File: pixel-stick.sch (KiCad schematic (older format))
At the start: 17 parts, among them J1 WS2811, J2 Conn_01x06, Q1 BSS138, U1 SPX3819M5-L-3-3, U2 RT9361AGE, U3 ESP-12E

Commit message: Layout board
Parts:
- C1: value 470µF -> 1000µF; footprint Capacitor_SMD:C_Elec_6.3x7.7 -> Capacitor_THT:CP_Radial_D10.0mm_P5.00mm
- J1: footprint Connector_Wire:SolderWirePad_1x03_P3.81mm_Drill1.2mm -> Connector_Wire:SolderWirePad_1x03_P3.175mm_Drill1mm
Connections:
- net +3V3: now also J2.2 (Pin_2); no longer J2.3 (Pin_3)
- net EN: now also J2.6 (Pin_6); no longer J2.2 (Pin_2)
- net GPIO0: now also J2.3 (Pin_3); no longer J2.6 (Pin_6)
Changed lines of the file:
@@
 EESchema Schematic File Version 4
 LIBS:pixel-stick-cache
-EELAYER 30 0
+EELAYER 29 0
 EELAYER END
 $Descr A4 11693 8268
@@
 P 5500 1750
 F 0 "C1" H 5615 1796 50  0000 L CNN
-F 1 "470µF" H 5615 1705 50  0000 L CNN
-F 2 "Capacitor_SMD:C_Elec_6.3x7.7" H 5500 1750 50  0001 C CNN
+F 1 "1000µF" H 5615 1705 50  0000 L CNN
+F 2 "Capacitor_THT:CP_Radial_D10.0mm_P5.00mm" H 5500 1750 50  0001 C CNN
 F 3 "~" H 5500 1750 50  0001 C CNN
 	1    5500 1750
@@
 F 0 "J1" H 2730 1642 50  0000 L CNN
 F 1 "WS2811" H 2730 1551 50  0000 L CNN
-F 2 "Connector_Wire:SolderWirePad_1x03_P3.81mm_Drill1.2mm" H 2650 1600 50  0001 C CNN
+F 2 "Connector_Wire:SolderWirePad_1x03_P3.175mm_Drill1mm" H 2650 1600 50  0001 C CNN
 F 3 "~" H 2650 1600 50  0001 C CNN
 	1    2650 1600
@@
 L power:+3.3V #PWR0106
 U 1 1 5E1A778D
-P 9700 4650
-F 0 "#PWR0106" H 9700 4500 50  0001 C CNN
-F 1 "+3.3V" V 9715 4778 50  0000 L CNN
-F 2 "" H 9700 4650 50  0001 C CNN
-F 3 "" H 9700 4650 50  0001 C CNN
-	1    9700 4650
+P 9700 4550
+F 0 "#PWR0106" H 9700 4400 50  0001 C CNN
+F 1 "+3.3V" V 9715 4678 50  0000 L CNN
+F 2 "" H 9700 4550 50  0001 C CNN
+F 3 "" H 9700 4550 50  0001 C CNN
+	1    9700 4550
 	0    -1   -1   0
 $EndComp
@@
 	10000 4450 9700 4450
 Wire Wire Line
+	10000 4550 9700 4550
+Wire Wire Line
+	10000 4950 9700 4950
+Wire Wire Line
+	10000 4750 9700 4750
+Wire Wire Line
+	10000 4850 9700 4850
+Wire Wire Line
 	10000 4650 9700 4650
-Wire Wire Line
-	10000 4550 9700 4550
-Wire Wire Line
-	10000 4750 9700 4750
-Wire Wire Line
-	10000 4850 9700 4850
-Wire Wire Line
-	10000 4950 9700 4950
 Text Label 9700 4750 0    50   ~ 0
 RXD
 Text Label 9700 4850 0    50   ~ 0
 TXD
-Text Label 9700 4550 0    50   ~ 0
+Text Label 9700 4950 0    50   ~ 0
 EN
-Text Label 9700 4950 0    50   ~ 0
+Text Label 9700 4650 0    50   ~ 0
 GPIO0
 Text Notes 9250 5500 0    157  ~ 0

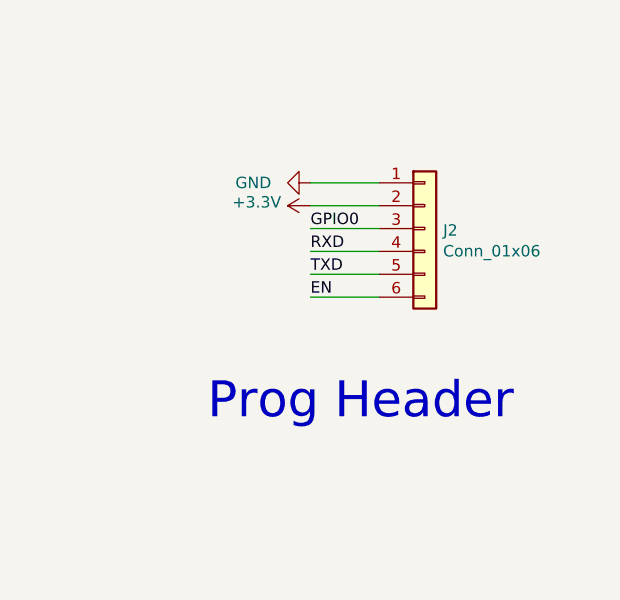
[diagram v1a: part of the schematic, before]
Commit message: revise board for testing
use the ESP-01 socket for most test points, added a 5V test point and changed the wire solder pads for 2.54mm pitch. Also added mounting (guide) holes for a test jig
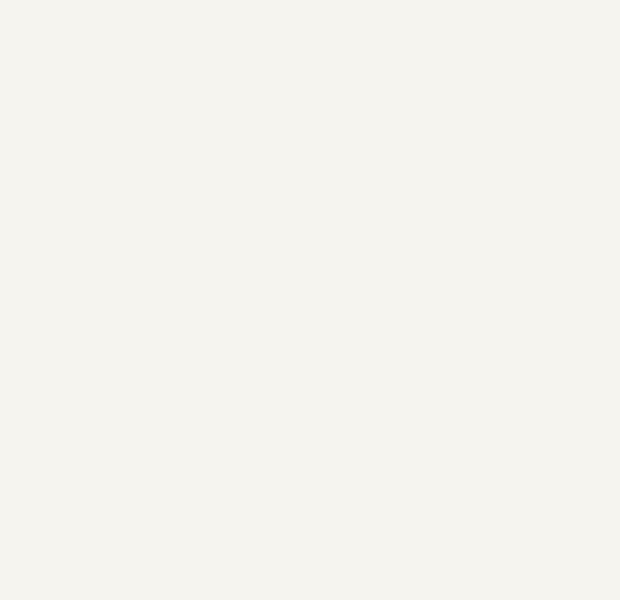
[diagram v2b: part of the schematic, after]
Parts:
- removed J2: Conn_01x06, Connector_PinHeader_2.54mm:PinHeader_1x06_P2.54mm_Vertical, symbol Connector_Generic:Conn_01x06
- J1: footprint Connector_Wire:SolderWirePad_1x03_P3.175mm_Drill1mm -> Connector_PinHeader_2.54mm:PinHeader_1x03_P2.54mm_Vertical
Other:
- note removed: "Prog Header"
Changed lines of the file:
@@
 EESchema Schematic File Version 4
 LIBS:pixel-stick-cache
-EELAYER 29 0
+EELAYER 30 0
 EELAYER END
 $Descr A4 11693 8268
@@
 F 0 "J1" H 2730 1642 50  0000 L CNN
 F 1 "WS2811" H 2730 1551 50  0000 L CNN
-F 2 "Connector_Wire:SolderWirePad_1x03_P3.175mm_Drill1mm" H 2650 1600 50  0001 C CNN
+F 2 "Connector_PinHeader_2.54mm:PinHeader_1x03_P2.54mm_Vertical" H 2650 1600 50  0001 C CNN
 F 3 "~" H 2650 1600 50  0001 C CNN
 	1    2650 1600
@@
 	1    0    0    -1
 $EndComp
-$Comp
-L Connector_Generic:Conn_01x06 J2
-U 1 1 5E1A6B59
-P 10200 4650
-F 0 "J2" H 10280 4642 50  0000 L CNN
-F 1 "Conn_01x06" H 10280 4551 50  0000 L CNN
-F 2 "Connector_PinHeader_2.54mm:PinHeader_1x06_P2.54mm_Vertical" H 10200 4650 50  0001 C CNN
-F 3 "~" H 10200 4650 50  0001 C CNN
-	1    10200 4650
-	1    0    0    -1
-$EndComp
-$Comp
-L power:+3.3V #PWR0106
-U 1 1 5E1A778D
-P 9700 4550
-F 0 "#PWR0106" H 9700 4400 50  0001 C CNN
-F 1 "+3.3V" V 9715 4678 50  0000 L CNN
-F 2 "" H 9700 4550 50  0001 C CNN
-F 3 "" H 9700 4550 50  0001 C CNN
-	1    9700 4550
-	0    -1   -1   0
-$EndComp
-$Comp
-L power:GND #PWR0107
-U 1 1 5E1A8422
-P 9700 4450
-F 0 "#PWR0107" H 9700 4200 50  0001 C CNN
-F 1 "GND" V 9700 4200 50  0000 C CNN
-F 2 "" H 9700 4450 50  0001 C CNN
-F 3 "" H 9700 4450 50  0001 C CNN
-	1    9700 4450
-	0    1    1    0
-$EndComp
-Wire Wire Line
-	10000 4450 9700 4450
-Wire Wire Line
-	10000 4550 9700 4550
-Wire Wire Line
-	10000 4950 9700 4950
-Wire Wire Line
-	10000 4750 9700 4750
-Wire Wire Line
-	10000 4850 9700 4850
-Wire Wire Line
-	10000 4650 9700 4650
-Text Label 9700 4750 0    50   ~ 0
-RXD
-Text Label 9700 4850 0    50   ~ 0
-TXD
-Text Label 9700 4950 0    50   ~ 0
-EN
-Text Label 9700 4650 0    50   ~ 0
-GPIO0
-Text Notes 9250 5500 0    157  ~ 0
-Prog Header
 Wire Wire Line
 	4300 3850 4650 3850

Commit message: shrink board
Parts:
- C1: value 1000µF -> 100µF; footprint Capacitor_THT:CP_Radial_D10.0mm_P5.00mm -> Capacitor_SMD:CP_Elec_6.3x7.7
- C2: value 1µF -> 10µF 16V
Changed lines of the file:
@@
 EESchema Schematic File Version 4
 LIBS:pixel-stick-cache
-EELAYER 30 0
+EELAYER 29 0
 EELAYER END
 $Descr A4 11693 8268
@@
 P 6300 1700
 F 0 "C2" H 6415 1746 50  0000 L CNN
-F 1 "1µF" H 6415 1655 50  0000 L CNN
+F 1 "10µF 16V" H 6415 1655 50  0000 L CNN
 F 2 "Capacitor_SMD:C_0805_2012Metric" H 6338 1550 50  0001 C CNN
 F 3 "~" H 6300 1700 50  0001 C CNN
@@
 P 5500 1750
 F 0 "C1" H 5615 1796 50  0000 L CNN
-F 1 "1000µF" H 5615 1705 50  0000 L CNN
-F 2 "Capacitor_THT:CP_Radial_D10.0mm_P5.00mm" H 5500 1750 50  0001 C CNN
+F 1 "100µF" H 5615 1705 50  0000 L CNN
+F 2 "Capacitor_SMD:CP_Elec_6.3x7.7" H 5500 1750 50  0001 C CNN
 F 3 "~" H 5500 1750 50  0001 C CNN
 	1    5500 1750

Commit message: rev 2.0a
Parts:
- J1: footprint Connector_PinHeader_2.54mm:PinHeader_1x03_P2.54mm_Vertical -> Connector_Wire:SolderWirePad_1x03_P3.175mm_Drill1mm
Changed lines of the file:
@@
 F 0 "J1" H 2730 1642 50  0000 L CNN
 F 1 "WS2811" H 2730 1551 50  0000 L CNN
-F 2 "Connector_PinHeader_2.54mm:PinHeader_1x03_P2.54mm_Vertical" H 2650 1600 50  0001 C CNN
+F 2 "Connector_Wire:SolderWirePad_1x03_P3.175mm_Drill1mm" H 2650 1600 50  0001 C CNN
 F 3 "~" H 2650 1600 50  0001 C CNN
 	1    2650 1600

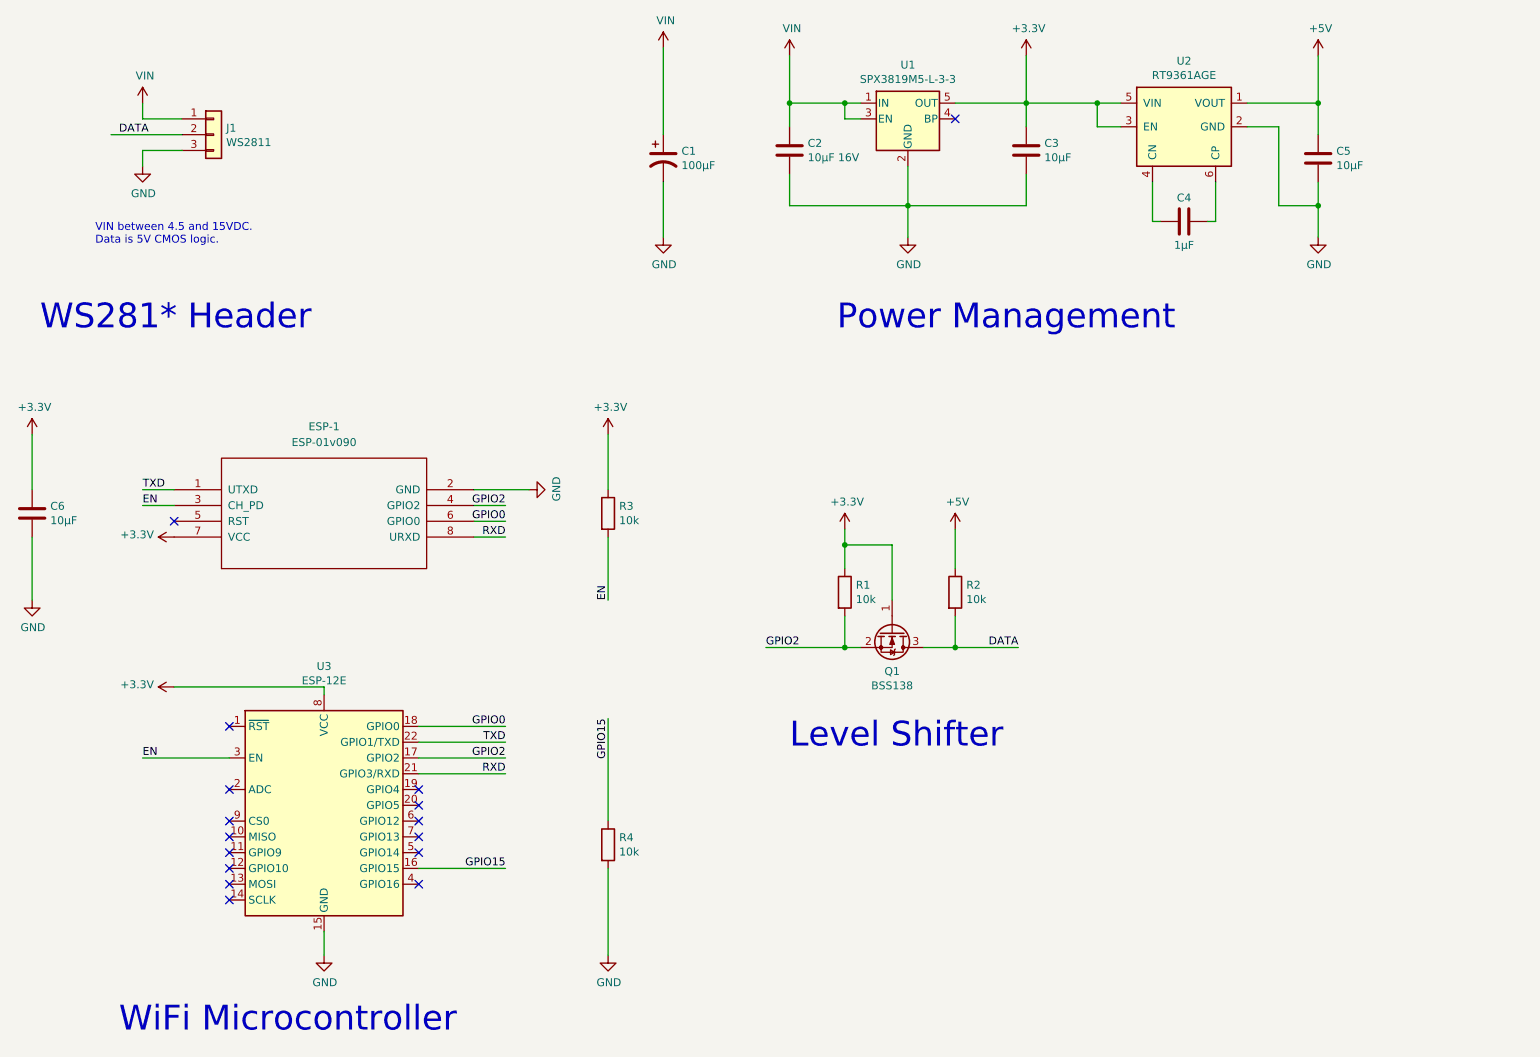
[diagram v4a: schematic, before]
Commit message: utilize level shifter
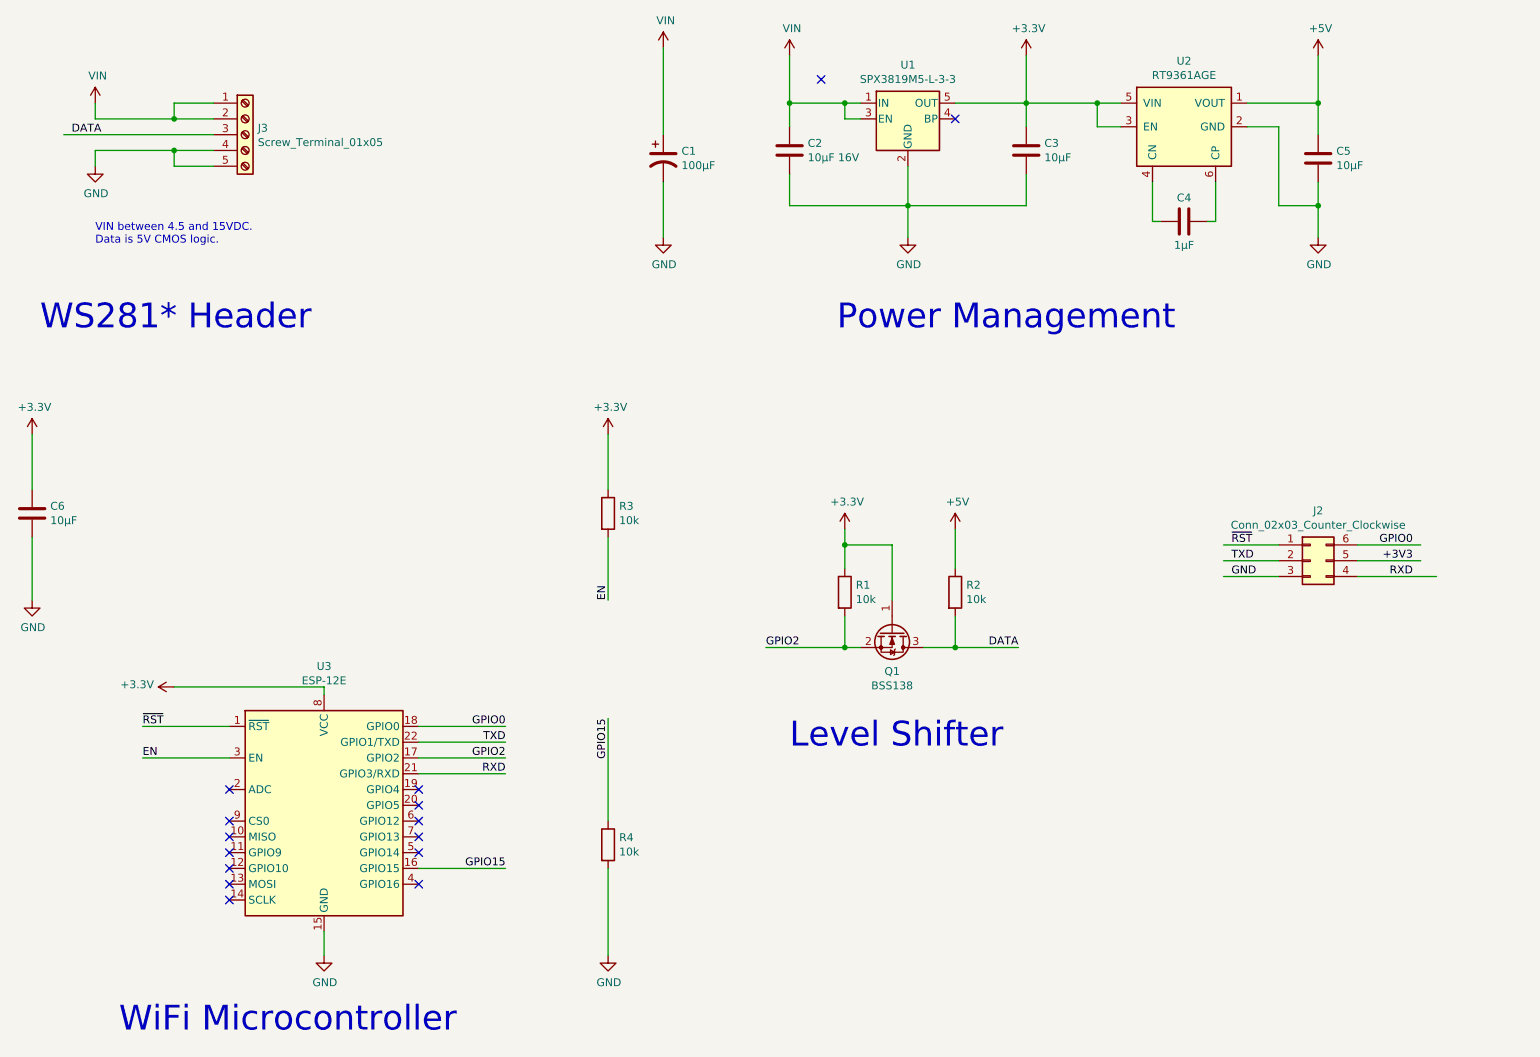
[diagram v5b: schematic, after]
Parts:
- removed ESP-1: ESP-01v090, ESP8266:ESP-01, symbol ESP8266:ESP-01v090
- removed J1: WS2811, Connector_Wire:SolderWirePad_1x03_P3.175mm_Drill1mm, symbol Connector_Generic:Conn_01x03
- added J2: Conn_02x03_Counter_Clockwise, Connector_PinHeader_2.54mm:PinHeader_2x03_P2.54mm_Vertical, symbol Connector_Generic:Conn_02x03_Counter_Clockwise
- added J3: Screw_Terminal_01x05, TerminalBlock_Phoenix:TerminalBlock_Phoenix_MPT-0,5-5-2.54_1x05_P2.54mm_Horizontal, symbol Connector:Screw_Terminal_01x05
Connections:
- net labels added: +3V3, ~RST
- wire segments 70 -> 77
- no-connect marks 16 -> 15
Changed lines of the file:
@@
 EESchema Schematic File Version 4
-LIBS:pixel-stick-cache
-EELAYER 29 0
+EELAYER 30 0
 EELAYER END
 $Descr A4 11693 8268
@@
 	1500 3500 1500 3850
 $Comp
-L power:+3.3V #PWR010
-U 1 1 5DEA7FFE
-P 2400 4150
-F 0 "#PWR010" H 2400 4000 50  0001 C CNN
-F 1 "+3.3V" V 2415 4278 50  0000 L CNN
-F 2 "" H 2400 4150 50  0001 C CNN
-F 3 "" H 2400 4150 50  0001 C CNN
-	1    2400 4150
-	0    -1   -1   0
-$EndComp
-Text Label 4500 4150 2    50   ~ 0
-RXD
-Text Label 2200 3850 0    50   ~ 0
-TXD
-Text Label 4500 4050 2    50   ~ 0
-GPIO0
-Text Label 4500 3950 2    50   ~ 0
-GPIO2
-Wire Wire Line
-	2400 3950 2200 3950
-Wire Wire Line
-	4500 4150 4300 4150
-Wire Wire Line
-	2200 3850 2400 3850
-Wire Wire Line
-	4300 4050 4500 4050
-Wire Wire Line
-	4300 3950 4500 3950
-$Comp
 L power:GND #PWR013
 U 1 1 5DEA0257
@@
 F 3 "~" H 1500 4000 50  0001 C CNN
 	1    1500 4000
-	1    0    0    -1
-$EndComp
-$Comp
-L ESP8266:ESP-01v090 ESP-1
-U 1 1 5DE9E498
-P 3350 4000
-F 0 "ESP-1" H 3350 4550 50  0000 C CNN
-F 1 "ESP-01v090" H 3350 4450 50  0000 C CNN
-F 2 "ESP8266:ESP-01" H 3350 4000 50  0001 C CNN
-F 3 "http://l0l.org.uk/2014/12/esp8266-modules-hardware-guide-gotta-catch-em-all/" H 3350 4000 50  0001 C CNN
-	1    3350 4000
 	1    0    0    -1
 $EndComp
@@
 $EndComp
 $Comp
-L Connector_Generic:Conn_01x03 J1
-U 1 1 5DFF0485
-P 2650 1600
-F 0 "J1" H 2730 1642 50  0000 L CNN
-F 1 "WS2811" H 2730 1551 50  0000 L CNN
-F 2 "Connector_Wire:SolderWirePad_1x03_P3.175mm_Drill1mm" H 2650 1600 50  0001 C CNN
-F 3 "~" H 2650 1600 50  0001 C CNN
-	1    2650 1600
-	1    0    0    -1
-$EndComp
-Text Label 2050 1600 0    50   ~ 0
-DATA
-Wire Wire Line
-	2000 1600 2450 1600
-$Comp
 L Transistor_FET:BSS138 Q1
 U 1 1 5E162D20
@@
 Wire Wire Line
 	6650 4200 6650 4100
-Text Label 2200 3950 0    50   ~ 0
-EN
 Wire Wire Line
 	5150 4150 5150 4550
@@
 GPIO2
 Wire Wire Line
-	3950 5350 4500 5350
-Wire Wire Line
 	3950 5550 4500 5550
 Text Label 4500 6250 2    50   ~ 0
@@
 	1    0    0    -1
 $EndComp
-Wire Wire Line
-	4300 3850 4650 3850
-$Comp
-L power:GND #PWR014
-U 1 1 5DEA2B31
-P 4650 3850
-F 0 "#PWR014" H 4650 3600 50  0001 C CNN
-F 1 "GND" H 4655 3677 50  0000 C CNN
-F 2 "" H 4650 3850 50  0001 C CNN
-F 3 "" H 4650 3850 50  0001 C CNN
-	1    4650 3850
-	0    -1   -1   0
-$EndComp
-NoConn ~ 2400 4050
-NoConn ~ 2750 5350
 NoConn ~ 2750 5750
 NoConn ~ 2750 5950
@@
 	1    0    0    -1
 $EndComp
-$Comp
-L pixel-stick:VIN #PWR0114
-U 1 1 5E1C5F60
-P 2200 1400
-F 0 "#PWR0114" H 2200 1250 50  0001 C CNN
-F 1 "VIN" H 2215 1573 50  0000 C CNN
-F 2 "" H 2200 1400 50  0001 C CNN
-F 3 "" H 2200 1400 50  0001 C CNN
-	1    2200 1400
-	1    0    0    -1
-$EndComp
-$Comp
-L power:GND #PWR0115
-U 1 1 5E1C6857
-P 2200 1800
-F 0 "#PWR0115" H 2200 1550 50  0001 C CNN
-F 1 "GND" H 2205 1627 50  0000 C CNN
-F 2 "" H 2200 1800 50  0001 C CNN
-F 3 "" H 2200 1800 50  0001 C CNN
-	1    2200 1800
-	1    0    0    -1
-$EndComp
-Wire Wire Line
-	2200 1800 2200 1700
-Wire Wire Line
-	2200 1700 2450 1700
-Wire Wire Line
-	2200 1400 2200 1500
-Wire Wire Line
-	2200 1500 2450 1500
 Text Notes 1550 2850 0    157  ~ 0
 WS281* Header
@@
 	6650 1400 6750 1400
 NoConn ~ 7350 1500
+Wire Wire Line
+	3950 5350 4500 5350
+NoConn ~ 6500 1250
+Wire Wire Line
+	2750 5350 2200 5350
+Text Label 2200 5350 0    50   ~ 0
+~RST
+Text Label 9100 4400 0    50   ~ 0
+GND
+Wire Wire Line
+	9400 4400 9050 4400
+Text Label 9100 4200 0    50   ~ 0
+~RST
+Wire Wire Line
+	9400 4200 9050 4200
+Text Label 10250 4400 2    50   ~ 0
+RXD
+Wire Wire Line
+	9900 4400 10400 4400
+Text Label 9100 4300 0    50   ~ 0
+TXD
+Wire Wire Line
+	9400 4300 9050 4300
+$Comp
+L Connector_Generic:Conn_02x03_Counter_Clockwise J2
+U 1 1 5FB87FB4
+P 9600 4300
+F 0 "J2" H 9650 4617 50  0000 C CNN
+F 1 "Conn_02x03_Counter_Clockwise" H 9650 4526 50  0000 C CNN
+F 2 "Connector_PinHeader_2.54mm:PinHeader_2x03_P2.54mm_Vertical" H 9600 4300 50  0001 C CNN
+F 3 "~" H 9600 4300 50  0001 C CNN
+	1    9600 4300
+	1    0    0    -1
+$EndComp
+Wire Wire Line
+	9900 4300 10300 4300
+Wire Wire Line
+	9900 4200 10300 4200
+Text Label 10250 4200 2    50   ~ 0
+GPIO0
+Text Label 10250 4300 2    50   ~ 0
++3V3
+$Comp
+L Connector:Screw_Terminal_01x05 J3
+U 1 1 5FD96649
+P 2850 1600
+F 0 "J3" H 2930 1642 50  0000 L CNN
+F 1 "Screw_Terminal_01x05" H 2930 1551 50  0000 L CNN
+F 2 "TerminalBlock_Phoenix:TerminalBlock_Phoenix_MPT-0,5-5-2.54_1x05_P2.54mm_Horizontal" H 2850 1600 50  0001 C CNN
+F 3 "~" H 2850 1600 50  0001 C CNN
+	1    2850 1600
+	1    0    0    -1
+$EndComp
+Text Label 1750 1600 0    50   ~ 0
+DATA
+$Comp
+L pixel-stick:VIN #PWR0106
+U 1 1 5FDBE78E
+P 1900 1400
+F 0 "#PWR0106" H 1900 1250 50  0001 C CNN
+F 1 "VIN" H 1915 1573 50  0000 C CNN
+F 2 "" H 1900 1400 50  0001 C CNN
+F 3 "" H 1900 1400 50  0001 C CNN
+	1    1900 1400
+	1    0    0    -1
+$EndComp
+$Comp
+L power:GND #PWR0107
+U 1 1 5FDBE794
+P 1900 1800
+F 0 "#PWR0107" H 1900 1550 50  0001 C CNN
+F 1 "GND" H 1905 1627 50  0000 C CNN
+F 2 "" H 1900 1800 50  0001 C CNN
+F 3 "" H 1900 1800 50  0001 C CNN
+	1    1900 1800
+	1    0    0    -1
+$EndComp
+Wire Wire Line
+	1900 1800 1900 1700
+Wire Wire Line
+	1900 1400 1900 1500
+Wire Wire Line
+	1700 1600 2650 1600
+Wire Wire Line
+	1900 1700 2400 1700
+Wire Wire Line
+	2650 1800 2400 1800
+Wire Wire Line
+	2400 1800 2400 1700
+Connection ~ 2400 1700
+Wire Wire Line
+	2400 1700 2650 1700
+Wire Wire Line
+	1900 1500 2400 1500
+Wire Wire Line
+	2650 1400 2400 1400
+Wire Wire Line
+	2400 1400 2400 1500
+Connection ~ 2400 1500
+Wire Wire Line
+	2400 1500 2650 1500
 $EndSCHEMATC
